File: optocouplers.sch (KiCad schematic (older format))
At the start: 20 parts, among them J901 Conn_01x04, Q901 MMBT5551L, U901 EL3H7(C)(TA)-G, U902 EL3H7(C)(TA)-G

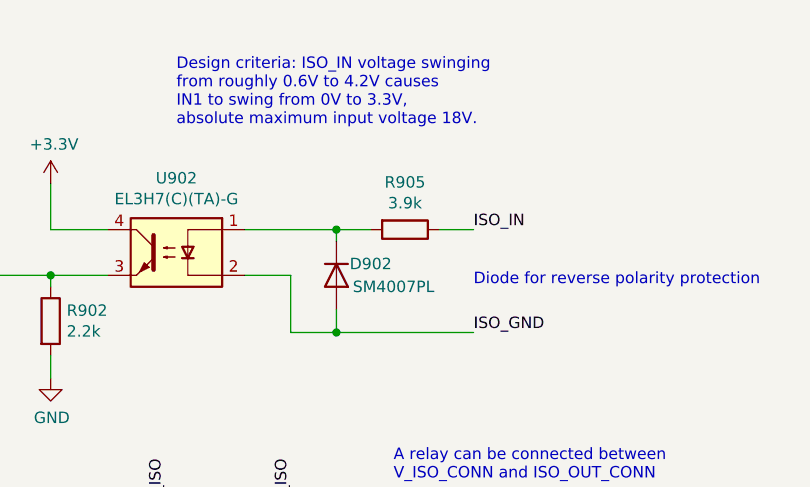
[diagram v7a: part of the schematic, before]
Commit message: Changed R905 to 0805 FP and value to 2.2k
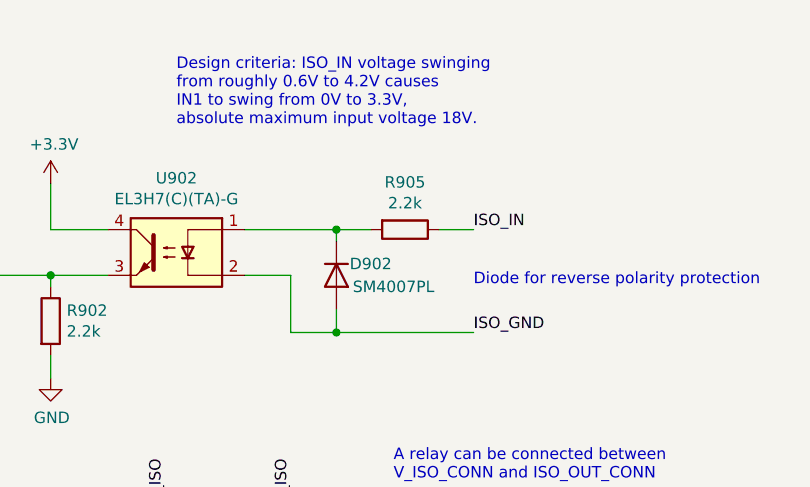
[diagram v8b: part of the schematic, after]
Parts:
- R905: value 3.9k -> 2.2k; footprint Resistor_SMD:R_0603_1608Metric -> Resistor_SMD:R_0805_2012Metric; LCSC C23018 -> C17520
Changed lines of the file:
@@
 $Descr A4 11693 8268
 encoding utf-8
-Sheet 11 11
+Sheet 10 11
 Title "Sailor Hat for ESP32"
 Date ""
@@
 P 4400 2300
 F 0 "R905" V 4193 2300 50  0000 C CNN
-F 1 "3.9k" V 4284 2300 50  0000 C CNN
-F 2 "Resistor_SMD:R_0603_1608Metric" V 4330 2300 50  0001 C CNN
+F 1 "2.2k" V 4284 2300 50  0000 C CNN
+F 2 "Resistor_SMD:R_0805_2012Metric" V 4330 2300 50  0001 C CNN
 F 3 "~" H 4400 2300 50  0001 C CNN
-F 4 "C23018" H 4400 2300 50  0001 C CNN "LCSC"
+F 4 "C17520" H 4400 2300 50  0001 C CNN "LCSC"
 	1    4400 2300
 	0    1    1    0
